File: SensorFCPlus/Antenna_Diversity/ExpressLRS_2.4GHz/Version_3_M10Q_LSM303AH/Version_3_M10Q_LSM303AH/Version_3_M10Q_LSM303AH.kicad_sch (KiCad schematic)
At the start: 31 parts, among them J1 Conn_01x05_Pin, J2 Conn_01x02_Pin, J3 Conn_01x05_Pin, J4 Conn_01x03_Pin, U1 LSM303AHTR, U2 SAM-M10Q-00B, U3 BAT54STA

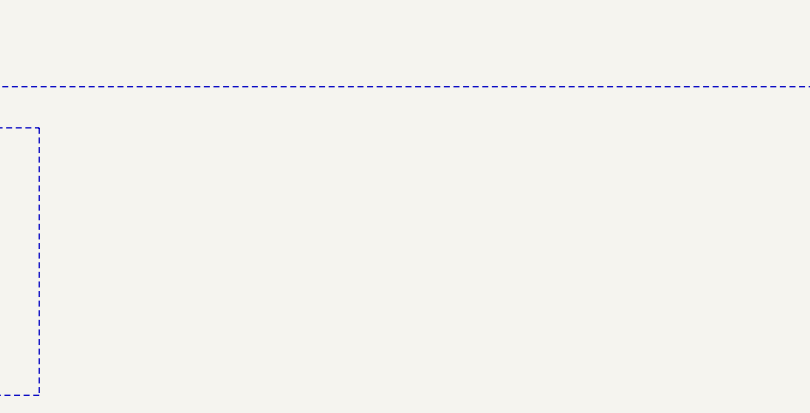
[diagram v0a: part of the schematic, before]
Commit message: Remove outdated KiCAD project files
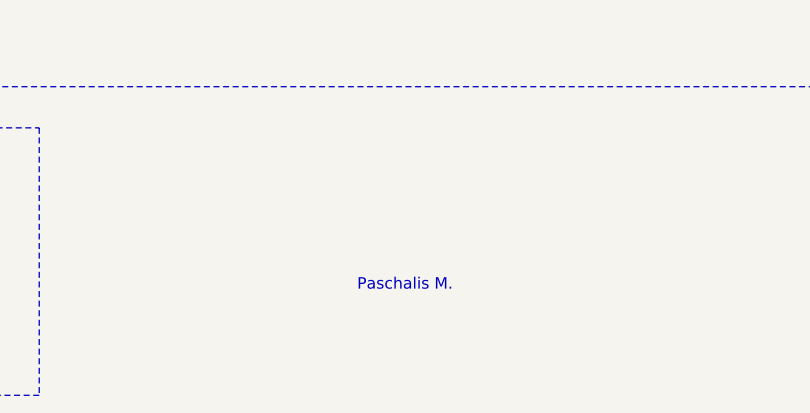
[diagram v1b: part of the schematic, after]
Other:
- note added: "Paschalis M."
- company: (none) -> https://github.com/Paschalis
- title: (none) -> Version 3 (GPS:M10Q, MAG:LSM303AH, ELRS:2.4GHz_RX)
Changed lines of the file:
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@@
 	(generator_version "8.0")
 	(paper "A4")
+	(title_block
+		(title "Version 3 (GPS:M10Q, MAG:LSM303AH, ELRS:2.4GHz_RX)")
+		(date "05-01-2025")
+		(rev "1.0")
+		(company "https://github.com/Paschalis")
+	)
 	(junction
 		(at 54.61 44.45)
@@
 		)
 	)
+	(image
+		(at 242.5 172.39)
+		(scale 0.098549)
+		(data "iVBORw0KGgoAAAANSUhEUgAAAWMAAAFjAQMAAADSDPiiAAAABlBMVEUAAAD///+l2Z/dAAAAAnRS"
+			"TlP//8i138cAAAAJcEhZcwAACxIAAAsSAdLdfvwAAAXxSURBVGiB3ZtBjrNKDIQbschyjpCbhItF"
+			"SqRcjNyEI2TJIoqf6yszM+9fPOlf+iENYugCKd1uu1w2I/7mGF3R+8hjXyK20zrm2MfXI/LqFqfn"
+			"67adPuO2JWTeEjU3Rguo37vty+t6js/XfeTpPeIZj8R8RZzCkEdj9CV/8H7J4X2K93mfXjkd8Zpz"
+			"Or7e57HE/ZzzlO/SZPVG23iX1xxe/uk1hHmPoasx5ez8D9C24EUGvcrc8y9tIE96LiFf7dHY95pr"
+			"m0udM/PJkVzvh3bxGJoiBv61Gxqi8VX86v88/fZs/dCYdi5rbtaL1naK+9CcbOPi6bjrhfPvKNUT"
+			"jfe9n9P7vs+xyqpl34m+5kkeWSvvd3VF7/K5J8WYPOXsTHpOzgnT1iMyDc1ORdem6Ff+f4E05Oxk"
+			"yLmOHMnpmPIqHRZh6KrlvzVGa21xTjk7bw1XsI2n0Ks2sCJuyJP1RY9c2wwvGVNl0Lhl7hV7CrZ3"
+			"aHTuiw7sVts2A41CbE7MLkMQH5TrSmt4ikh4z/dFJ3vX2iaHECsSSVrARMXZYcoo++6Kli3LOcVm"
+			"7qdImtNhmluWLi+dz0VrdPgmLMGsV/4L08571zNOLNbDV/VE5xkOMcRrvZXF/ULP2WHJvtMtd0Zj"
+			"y6EQK8KrU5CDilfklCg5Ff8dB4doieYHyyNvXDExAy99MQs8PLLe0BZ9cHvpJ1p5sV7Wm1gERxSF"
+			"Ymf3RRN3Epg3P3oQrssj3wJRkKEe/rslOqfjPg4p4U60kcPKrbx+QYLfYvnkpY3Ruco3eSgdijFo"
+			"YahEoZw7EMR8tEZL0pRfYoGHgq33s5mwiOKk1AY20RXNZs3hWQQ/N6tSlhyGH4kzyYkFjxB3uqJz"
+			"RS0B7Qh7kMKL9+4N33xGOao8rSv6IvpwIYgqxthN6V+laFKrKyqtldX1RC8k2db57rq6y76vZy+/"
+			"TFvvIvg0RosbsN7S3816ofoOSHJYVuetn3RFQx+wb13JtF07QpiXFiYKpVTOVZWe6LRbLTWrLL1I"
+			"toyHItQwKlq/WWfpimbbOtOe0Gx1szI2jmtRqMX+uyfaQQXtYGIXMwJdUpz9fNNhZwJN0QYuzsSK"
+			"wluPtqtWBHrGT9zpi+YHyznhl0pUcA46DhH+p57WEs10aNvmAt8HG7jyFldahNZjU0WpnmhJJxi5"
+			"6isuIIWUeCRcc/vJ5t4YDStyvcHkNti7qiKRoWqUFzpP64rWTNBN4ZSlNjATM9xwQZGl5qQpGv0k"
+			"V34ovFQ/wiGdPIrbP3lXZTA90ZA9avGfUmphvUTcgUAER7QU2BUd9BmsqLcqrWDVK7qm6mKcxJRc"
+			"eWiLVuMI6u3OKsdLGvWLjhJqnFJSvpX4vmhXNgcpmm4SXeWwxq02MM0k7rVoij5KDW+Cz3Y4p7na"
+			"2/QwDvpXdG2IltY+KHTqFFg6DQgWyUR4KRDuxe17omGz6AlSoTcLYtq29lpVQLqJOD36oitHofpn"
+			"nQ85xWWU7aCHOO25MbpYINye3pKr/RdeK57uHXqYR7VFQ9xdMimm9K7suwoqzrnPR3WiLfp6pvnS"
+			"IWeFOEVJfEiaoMelNXpYCyNFY71vmzuBJtd0oRT3YWmsKxqlFm9U9epXOScK8hDF4sRVue6JFoew"
+			"PF19JIjSFD+xBnpp5Kpfc2N0oLrT2x4UGCiYvRlwjzTWX7yqLVqmfeHLC6qdoviq7o7Jvadh1vud"
+			"u/ZEV6laPaX+JONeISds88dW/nRGU5+nKo+vcsP34iTbGUz1DpkPdkUvDi9X9RnopOrf6q5+6HB9"
+			"ZzSsUbdFO2+527TdRsPeZXhQICzpsy/aslCl1qqQ6Zsi+C9o6km0Ihw98S3R1sLkh/lOAdpnCZfi"
+			"J1+krGP+qeb3RC/EVJZajJ4C9eKy4I1efidrzdH1VRgp2uyv+WwIksH8hZ/rK/3Rz+ILTttMJEQA"
+			"T6VwfmvUrdGrRAWaoknHlLtZIKKkvRTNaIxe3F75sHZAwYz+PYoO+/JHpakrunwVGvVMc0U1fn1z"
+			"xJNFo5/qRD90/M3RFf0P9E1dEMR0b2wAAAAASUVORK5CYII="
+		)
+	)
 	(text_box "R=(V_battery-V_f-V_chagre)/I_charge=(3.7-0.24-3.0)/0.0001=4.6K (4.7K)"
 		(exclude_from_sim no)
@@
 			)
 		)
+	)
+	(text "Paschalis M."
+		(exclude_from_sim no)
+		(at 214.63 183.388 0)
+		(effects
+			(font
+				(size 1.27 1.27)
+			)
+		)

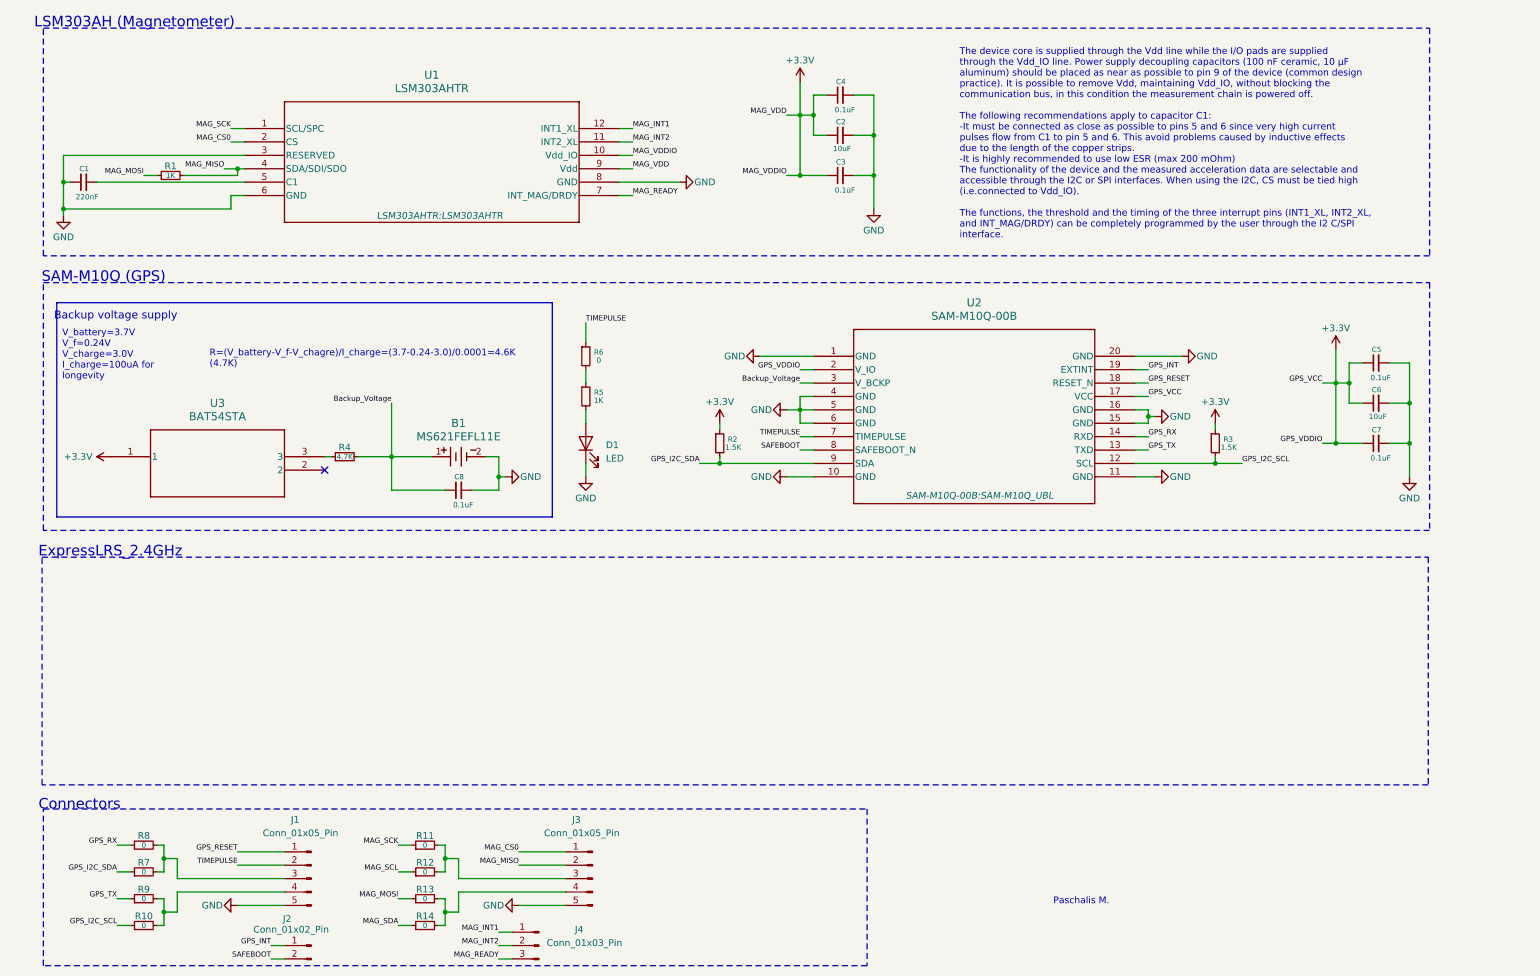
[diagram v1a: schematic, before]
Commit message: Update KiCad files for ExpressLRS modules
- Modified:
  - 2.4GHz Version 3 (M10Q LSM303AH) project and schematic files
  - 900MHz Version 3 (M10Q LSM303AH) schematic files for ESP8285 and SE2435L

- Added:
  - 2.4GHz Version 3 schematics: ESP8285, SE2431, SE2431L, SX1280
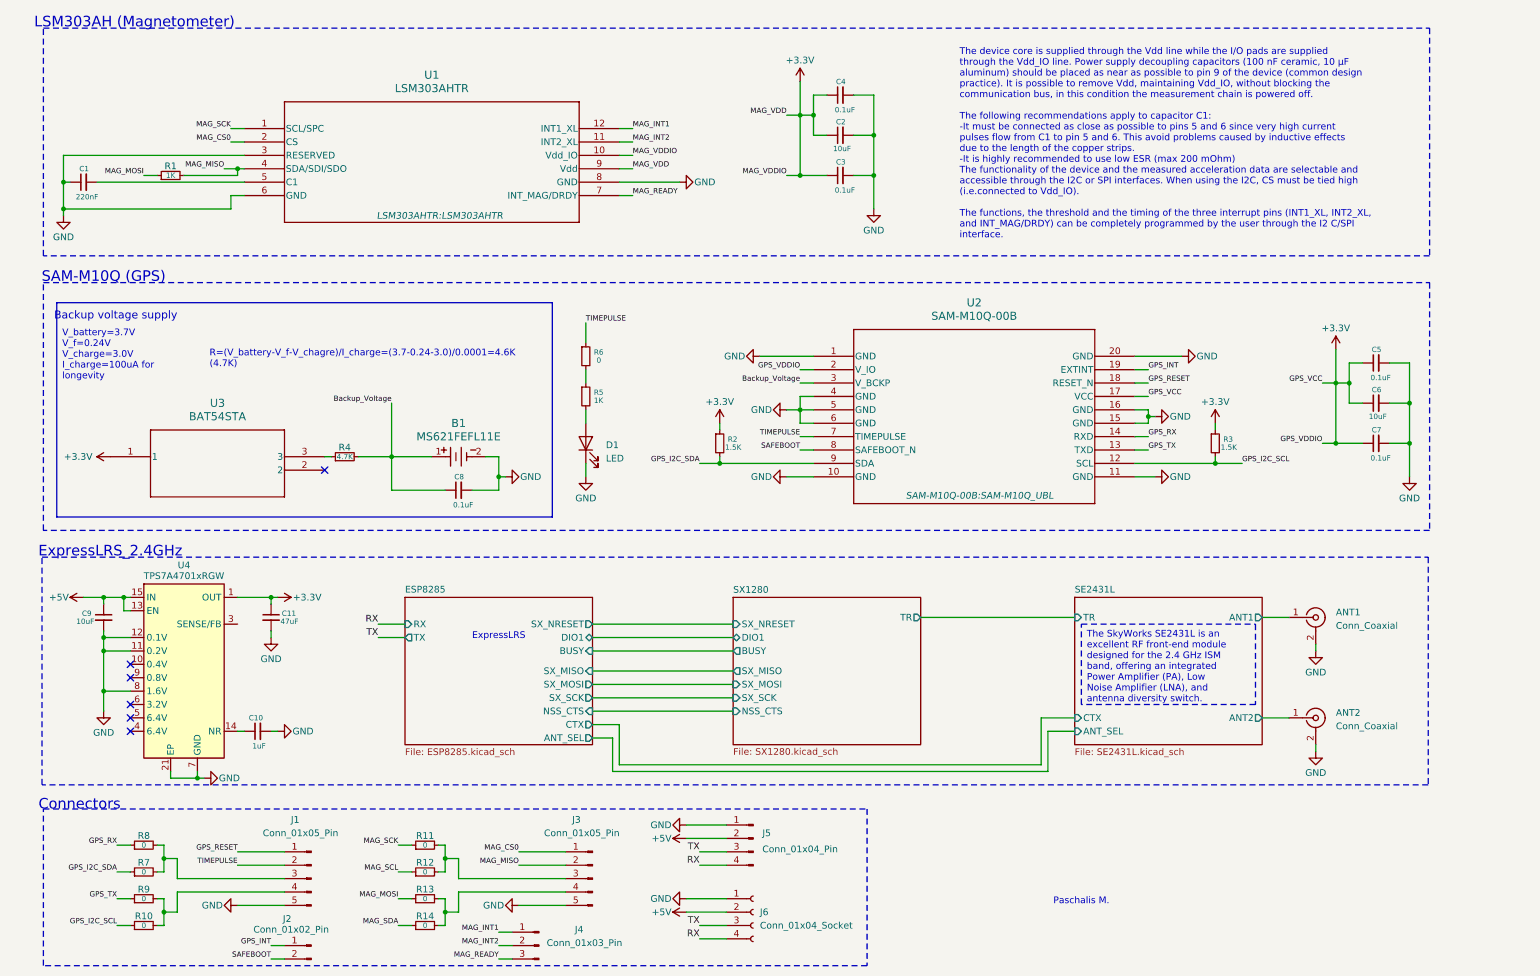
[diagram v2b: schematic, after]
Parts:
- added ANT1, ANT2: Conn_Coaxial, Connector_Coaxial:U.FL_Hirose_U.FL-R-SMT-1_Vertical, symbol Connector:Conn_Coaxial
- added C10: 1uF, Capacitor_SMD:C_0805_2012Metric_Pad1.18x1.45mm_HandSolder, symbol Device:C_Small
- added C11: 47uF, Capacitor_SMD:C_0805_2012Metric_Pad1.18x1.45mm_HandSolder, symbol Device:C_Small
- added C9: 10uF, Capacitor_SMD:C_0805_2012Metric_Pad1.18x1.45mm_HandSolder, symbol Device:C_Small
- added J5: Conn_01x04_Pin, Connector_JST:JST_GH_SM04B-GHS-TB_1x04-1MP_P1.25mm_Horizontal, symbol Connector:Conn_01x04_Pin
- added J6: Conn_01x04_Socket, Connector_Harwin:Harwin_M20-89004xx_1x04_P2.54mm_Horizontal, symbol Connector:Conn_01x04_Socket
- added U4: TPS7A4701xRGW, Package_DFN_QFN:Texas_RGW0020A_VQFN-20-1EP_5x5mm_P0.65mm_EP3.15x3.15mm_ThermalVias, symbol Regulator_Linear:TPS7A4701xRGW
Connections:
- net +3.3V: now also C11.1, U4.1 (OUT), U4.20 (OUT)
- net GND: now also ANT1.2 (Ext), ANT2.2 (Ext), C10.2, C11.2, C9.2, J5.1 (Pin_1), J6.1 (Pin_1), U4.11 (0.2V), U4.12 (0.1V), U4.21 (EP), U4.7 (GND), U4.8 (1.6V)
- new net: C10.1, U4.14 (NR)
- new net +5V: C9.1, J5.2 (Pin_2), J6.2 (Pin_2), U4.13 (EN), U4.15 (IN), U4.16 (IN)
- new net RX: J5.4 (Pin_4), J6.4 (Pin_4)
- new net SE2431L/ANT1: ANT1.1 (In)
- new net SE2431L/ANT2: ANT2.1 (In)
- new net TX: J5.3 (Pin_3), J6.3 (Pin_3)
- no-connect marks 1 -> 6
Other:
- added sheet ESP8285 (ESP8285.kicad_sch)
- added sheet SE2431L (SE2431L.kicad_sch)
- added sheet SX1280 (SX1280.kicad_sch)
- note added: "ExpressLRS"

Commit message: Update PCB design for Version 3 M10Q LSM303AH (ESP8285, SE2431L, SX1280, and main board)
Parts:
- C1, C3, C4: footprint Capacitor_SMD:C_0805_2012Metric_Pad1.18x1.45mm_HandSolder -> Capacitor_SMD:C_0603_1608Metric_Pad1.08x0.95mm_HandSolder
- J4: footprint Connector_PinHeader_2.00mm:PinHeader_1x02_P2.00mm_Vertical -> Connector_PinHeader_2.00mm:PinHeader_1x03_P2.00mm_Vertical
- R1, R10, R11, R12, R13, R14, R7, R8, R9: footprint Resistor_SMD:R_0805_2012Metric_Pad1.20x1.40mm_HandSolder -> Resistor_SMD:R_0603_1608Metric_Pad0.98x0.95mm_HandSolder
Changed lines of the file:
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@@
 			)
 		)
-		(property "Footprint" "Resistor_SMD:R_0805_2012Metric_Pad1.20x1.40mm_HandSolder"
+		(property "Footprint" "Resistor_SMD:R_0603_1608Metric_Pad0.98x0.95mm_HandSolder"
 			(at 41.91 45.72 0)
 			(effects
@@
 			)
 		)
-		(property "Footprint" "Resistor_SMD:R_0805_2012Metric_Pad1.20x1.40mm_HandSolder"
+		(property "Footprint" "Resistor_SMD:R_0603_1608Metric_Pad0.98x0.95mm_HandSolder"
 			(at 36.83 182.88 0)
 			(effects
@@
 			)
 		)
-		(property "Footprint" "Connector_PinHeader_2.00mm:PinHeader_1x02_P2.00mm_Vertical"
+		(property "Footprint" "Connector_PinHeader_2.00mm:PinHeader_1x03_P2.00mm_Vertical"
 			(at 111.76 191.77 0)
 			(effects
@@
 			)
 		)
-		(property "Footprint" "Capacitor_SMD:C_0805_2012Metric_Pad1.18x1.45mm_HandSolder"
+		(property "Footprint" "Capacitor_SMD:C_0603_1608Metric_Pad1.08x0.95mm_HandSolder"
 			(at 25.4 46.99 0)
 			(effects
@@
 			)
 		)
-		(property "Footprint" "Resistor_SMD:R_0805_2012Metric_Pad1.20x1.40mm_HandSolder"
+		(property "Footprint" "Resistor_SMD:R_0603_1608Metric_Pad0.98x0.95mm_HandSolder"
 			(at 90.17 182.88 0)
 			(effects
@@
 			)
 		)
-		(property "Footprint" "Resistor_SMD:R_0805_2012Metric_Pad1.20x1.40mm_HandSolder"
+		(property "Footprint" "Resistor_SMD:R_0603_1608Metric_Pad0.98x0.95mm_HandSolder"
 			(at 90.17 187.96 0)
 			(effects
@@
 			)
 		)
-		(property "Footprint" "Resistor_SMD:R_0805_2012Metric_Pad1.20x1.40mm_HandSolder"
+		(property "Footprint" "Resistor_SMD:R_0603_1608Metric_Pad0.98x0.95mm_HandSolder"
 			(at 90.17 172.72 0)
 			(effects
@@
 			)
 		)
-		(property "Footprint" "Resistor_SMD:R_0805_2012Metric_Pad1.20x1.40mm_HandSolder"
+		(property "Footprint" "Resistor_SMD:R_0603_1608Metric_Pad0.98x0.95mm_HandSolder"
 			(at 36.83 177.8 0)
 			(effects
@@
 			)
 		)
-		(property "Footprint" "Resistor_SMD:R_0805_2012Metric_Pad1.20x1.40mm_HandSolder"
+		(property "Footprint" "Resistor_SMD:R_0603_1608Metric_Pad0.98x0.95mm_HandSolder"
 			(at 36.83 172.72 0)
 			(effects
@@
 			)
 		)
-		(property "Footprint" "Capacitor_SMD:C_0805_2012Metric_Pad1.18x1.45mm_HandSolder"
+		(property "Footprint" "Capacitor_SMD:C_0603_1608Metric_Pad1.08x0.95mm_HandSolder"
 			(at 168.91 45.72 0)
 			(effects
@@
 			)
 		)
-		(property "Footprint" "Resistor_SMD:R_0805_2012Metric_Pad1.20x1.40mm_HandSolder"
+		(property "Footprint" "Resistor_SMD:R_0603_1608Metric_Pad0.98x0.95mm_HandSolder"
 			(at 90.17 177.8 0)
 			(effects
@@
 			)
 		)
-		(property "Footprint" "Resistor_SMD:R_0805_2012Metric_Pad1.20x1.40mm_HandSolder"
+		(property "Footprint" "Resistor_SMD:R_0603_1608Metric_Pad0.98x0.95mm_HandSolder"
 			(at 36.83 187.96 0)
 			(effects
@@
 			)
 		)
-		(property "Footprint" "Capacitor_SMD:C_0805_2012Metric_Pad1.18x1.45mm_HandSolder"
+		(property "Footprint" "Capacitor_SMD:C_0603_1608Metric_Pad1.08x0.95mm_HandSolder"
 			(at 168.91 30.48 0)
 			(effects
